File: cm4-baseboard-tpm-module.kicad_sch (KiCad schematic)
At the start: 0 parts

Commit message: [#104798] Add SLB9672 and gpio connector to schematic
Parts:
- added C1, C2, C4: C_100n_25V_0402, antmicro-footprints:C_0402_1005Metric, symbol antmicroCapacitors0402:C_100n_25V_0402
- added C3: C_1u_10V_X7R_0402, antmicro-footprints:C_0402_1005Metric, symbol antmicroCapacitors0402:C_1u_10V_X7R_0402
- added J1: Plug_Samtec_ERM5_2x20_ERM5-020-05.0-L-DV-K-TR, antmicro-footprints:Conn_Plug_Samtec_ERM5_2x20_ERM5-020-05.0-L-DV-K-TR, symbol antmicroB2BConnectors:Plug_Samtec_ERM5_2x20_ERM5-020-05.0-L-DV-K-TR
- added R1, R2, R3, R4, R5, R6, R7, R8, R9: R_0R_0402, antmicro-footprints:R_0402_1005Metric, symbol antmicroResistors0402:R_0R_0402
- added U1: OPTIGA TPM SLB 9672 FW16, antmicro-footprints:QFN-32-1EP_5x5mm, symbol antmicroInterfaceControllers:OPTIGA TPM SLB 9672 FW16
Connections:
- new net: U1.10 (NCI_3), U1.11 (NCI_4), U1.12 (NCI_5), U1.13 (NCI_6), U1.15 (NCI_7), U1.16 (NCI_8/GND), U1.25 (NCI_9), U1.26 (NCI_10), U1.27 (NCI_11), U1.28 (NCI_12), U1.31 (NCI_13), U1.5 (NCI_1), U1.8 (NCI_2/VDD)
- new net: U1.29 (NC2), U1.30 (NC3), U1.6 (NC1)
- new net +3V3: C1.2, C2.2, C3.2, C4.2, J1.1, J1.17, U1.1 (VDD_1), U1.14 (VDD_2), U1.22 (VDD_3)
- new net GND: C1.1, C2.1, C3.1, C4.1, J1.20, J1.25, J1.34, J1.39, J1.6, J1.9, U1.2 (GND_1), U1.23 (GND_3), U1.32 (GND_4), U1.33 (EP), U1.9 (GND_2)
- new net GPIO.0/SDA0: J1.27
- new net GPIO.10: J1.19
- new net GPIO.11: J1.23
- new net GPIO.12/RXD5: J1.32
- new net GPIO.13/TXD5: J1.33
- new net GPIO.14/RXD0: J1.8
- new net GPIO.15/TXD0: J1.10
- new net GPIO.16: J1.36
- new net GPIO.17: J1.11
- new net GPIO.18: J1.12
- new net GPIO.19: J1.35
- new net GPIO.1/SCL0: J1.28
- new net GPIO.2: J1.3
- new net GPIO.20: J1.38
- new net GPIO.21: J1.40
- new net GPIO.22: J1.15
- new net GPIO.23: J1.16
- new net GPIO.24: J1.18
- new net GPIO.25: J1.22
- new net GPIO.26: J1.37
- new net GPIO.27: J1.13
- new net GPIO.3: J1.5
- new net GPIO.4/TXD3: J1.7
- new net GPIO.5/RXD3: J1.29
- new net GPIO.6: J1.31
- new net GPIO.7: J1.26
- new net GPIO.8/TXD4: J1.24
- new net GPIO.9/RXD4: J1.21
- new net GPIO.AIN0: J1.30
- new net GPIO.AIN1: J1.14
- new net GPIO_00: R7.2, U1.3 (GPIO__00)
- new net GPIO_00_R: R7.1
- new net GPIO_01: R8.2, U1.4 (GPIO__01)
- new net GPIO_01_R: R8.1
- new net GPIO_02: R9.2, U1.7 (GPIO__02)
- new net GPIO_02_R: R9.1
- new net SPI.MISO: R3.2, U1.24 (MISO)
- new net SPI.MISO_R: R3.1
- new net SPI.MOSI: R4.2, U1.21 (MOSI)
- new net SPI.MOSI_R: R4.1
- new net SPI.SCLK: R1.2, U1.19 (SCLK)
- new net SPI.SCLK_R: R1.1
- new net SPI.~{CS}: R2.2, U1.20 (CS_N)
- new net SPI.~{CS}_R: R2.1
- new net ~{PIRQ}: R5.2, U1.18 (PIRQ_N)
- new net ~{PIRQ}_R: R5.1
- new net ~{RST}: R6.2, U1.17 (RST_N)
- new net ~{RST}_R: R6.1
- no-connect marks 0 -> 4
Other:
- note added: "5V not supported"
- note added: "CM4 Baseboard connector"
- note added: "Connect to suitable GPIO!"
- note added: "Pin 8 Pulled up to 3V3"
- note added: "Pullup on CS"
- note added: "Symbol and Footprint both need to be changed! Design stays intact"
- note added: "https://www.infineon.com/assets/row/public/documents/30/49/infineon-slb9672-tpm20-spi-fw16.xx-ds-rev1-3-2024-11-18-datasheet-en.pdf https://www.mouser.pl/datasheet/3/70/1/infineon_optiga_tpm_slb_9672_kit_datasheet_en.pdf"

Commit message: [#104798] Update SLB9672 symbol, finish schematic
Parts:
- removed U1: OPTIGA TPM SLB 9672 FW16, antmicro-footprints:QFN-32-1EP_5x5mm, symbol antmicroInterfaceControllers:OPTIGA TPM SLB 9672 FW16
- added C5: C_100n_25V_0402, antmicro-footprints:C_0402_1005Metric, symbol antmicroCapacitors0402:C_100n_25V_0402
- added R10, R11: R_10k_0402, antmicro-footprints:R_0402_1005Metric, symbol antmicroResistors0402:R_10k_0402
- added U2: SLB9672XU20FW1624XTMA1, antmicro-footprints:QFN-32-1EP_5x5mm_P0.5mm, symbol antmicroInterfaceControllers:SLB9672XU20FW1624XTMA1
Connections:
- net GPIO.10 is gone; now on net SPI.SCLK: J1.19
- net GPIO.11 is gone; now on net SPI.SCLK: J1.23
- net GPIO.8/TXD4 is gone; now on net SPI.~{CS}: J1.24
- net GPIO.9/RXD4 is gone; now on net SPI.MISO: J1.21
- net +3V3: now also C5.2, R10.2, R11.2, U2.1 (VDD), U2.14 (VDD), U2.22 (VDD), U2.8 (NCI/VDD)
- net GND: now also C5.1, U2.16 (NCI/GND), U2.33 (EP), U2.[2,9,23,32] (GND)
- net GPIO_00: now also R7.1; no longer R7.2
- net GPIO_00_R: now also R7.2, U2.3 (GPIO__00); no longer R7.1
- net GPIO_01: now also R8.1; no longer R8.2
- net GPIO_01_R: now also R8.2, U2.4 (GPIO__01); no longer R8.1
- net GPIO_02: now also R9.1; no longer R9.2
- net GPIO_02_R: now also R9.2, U2.7 (GPIO__02); no longer R9.1
- net SPI.MISO: now also R3.1; no longer R3.2
- net SPI.MISO_R: now also R3.2, U2.24 (MISO); no longer R3.1
- net SPI.MOSI: now also R4.1; no longer R4.2
- net SPI.MOSI_R: now also R4.2, U2.21 (MOSI); no longer R4.1
- net SPI.SCLK: now also R1.1; no longer R1.2
- net SPI.SCLK_R: now also R1.2, U2.19 (SCLK); no longer R1.1
- net SPI.~{CS}: now also R2.1; no longer R2.2
- net SPI.~{CS}_R: now also R2.2, R10.1, U2.20 (~{CS}); no longer R2.1
- net ~{PIRQ}: now also R5.1; no longer R5.2
- net ~{PIRQ}_R: now also R5.2, U2.18 (~{PIRQ}); no longer R5.1
- net ~{RST}: now also R6.1; no longer R6.2
- net ~{RST}_R: now also R6.2, U2.17 (~{RST}); no longer R6.1
- new net: R11.1, U2.10 (NCI/VDD)
- no-connect marks 4 -> 2
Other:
- note added: "Connect to any GPIO for easier routing"
- note added: "SLB9672 TPM IC"
- note removed: "Connect to suitable GPIO!"
- note removed: "Pin 8 Pulled up to 3V3"
- note removed: "Pullup on CS"
- note removed: "Symbol and Footprint both need to be changed! Design stays intact"
- note removed: "https://www.infineon.com/assets/row/public/documents/30/49/infineon-slb9672-tpm20-spi-fw16.xx-ds-rev1-3-2024-11-18-datasheet-en.pdf https://www.mouser.pl/datasheet/3/70/1/infineon_optiga_tpm_slb_9672_kit_datasheet_en.pdf"
- moved on the sheet: C1, C2, C3, C4, J1, R1, R2, R3, R4, R5, R6, R7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

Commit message: [#104798] Make full placement and layout, clear DRC
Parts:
- added N1001: antmicro_logo, antmicro-footprints:antmicro-logo_scaled_12mm, symbol antmicroMechanicalParts:antmicro_logo
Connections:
- net GPIO.14/RXD0 is gone; now on net ~{RST}: J1.8
- net GPIO.15/TXD0 is gone; now on net ~{PIRQ}: J1.10
- net GPIO.16 is gone; now on net GPIO_00: J1.36
- net GPIO.20 is gone; now on net GPIO_01: J1.38
- net GPIO.21 is gone; now on net GPIO_02: J1.40
- net SPI.MOSI: now also J1.19
- net SPI.SCLK: no longer J1.19
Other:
- note removed: "Connect to any GPIO for easier routing"
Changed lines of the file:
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@@
 		)
 	)
-	(text "Connect to any GPIO for easier routing"
-		(exclude_from_sim no)
-		(at 187.452 161.036 0)
-		(effects
-			(font
-				(size 1.27 1.27)
-			)
-		)
-	)
 	(junction
 		(at 303.53 124.46)
@@
 	(wire
 		(pts
-			(xy 142.24 161.29) (xy 160.02 161.29)
-		)
-		(stroke
-			(width 0)
-			(type default)
-		)
-	)
-	(wire
-		(pts
 			(xy 209.55 163.83) (xy 222.25 163.83)
 		)
@@
 		)
 	)
-	(wire
-		(pts
-			(xy 142.24 158.75) (xy 160.02 158.75)
-		)
-		(stroke
-			(width 0)
-			(type default)
-		)
-	)
 	(bus
 		(pts
@@
 	(wire
 		(pts
+			(xy 142.24 161.29) (xy 160.02 161.29)
+		)
+		(stroke
+			(width 0)
+			(type default)
+		)
+	)
+	(wire
+		(pts
 			(xy 142.24 135.89) (xy 160.02 135.89)
 		)
@@
 	(wire
 		(pts
-			(xy 113.03 161.29) (xy 130.81 161.29)
+			(xy 142.24 158.75) (xy 160.02 158.75)
 		)
 		(stroke
@@
 	(wire
 		(pts
-			(xy 209.55 157.48) (xy 222.25 157.48)
+			(xy 113.03 161.29) (xy 130.81 161.29)
 		)
 		(stroke
@@
 	(wire
 		(pts
-			(xy 332.74 133.35) (xy 332.74 135.89)
+			(xy 209.55 157.48) (xy 222.25 157.48)
 		)
 		(stroke
@@
 	(wire
 		(pts
-			(xy 113.03 158.75) (xy 130.81 158.75)
+			(xy 332.74 133.35) (xy 332.74 135.89)
 		)
 		(stroke
@@
 	(wire
 		(pts
-			(xy 303.53 133.35) (xy 303.53 132.08)
+			(xy 113.03 158.75) (xy 130.81 158.75)
 		)
 		(stroke
@@
 	(wire
 		(pts
-			(xy 227.33 154.94) (xy 247.65 154.94)
+			(xy 303.53 133.35) (xy 303.53 132.08)
 		)
 		(stroke
@@
 	(wire
 		(pts
-			(xy 227.33 157.48) (xy 247.65 157.48)
+			(xy 227.33 154.94) (xy 247.65 154.94)
 		)
 		(stroke
@@
 	(wire
 		(pts
-			(xy 113.03 168.91) (xy 130.81 168.91)
+			(xy 227.33 157.48) (xy 247.65 157.48)
 		)
 		(stroke
@@
 	(wire
 		(pts
-			(xy 142.24 156.21) (xy 160.02 156.21)
+			(xy 113.03 168.91) (xy 130.81 168.91)
 		)
 		(stroke
@@
 	(wire
 		(pts
-			(xy 113.03 163.83) (xy 130.81 163.83)
+			(xy 142.24 153.67) (xy 160.02 153.67)
 		)
 		(stroke
@@
 	(wire
 		(pts
-			(xy 142.24 153.67) (xy 160.02 153.67)
+			(xy 113.03 163.83) (xy 130.81 163.83)
 		)
 		(stroke
@@
 	(wire
 		(pts
+			(xy 142.24 156.21) (xy 160.02 156.21)
+		)
+		(stroke
+			(width 0)
+			(type default)
+		)
+	)
+	(wire
+		(pts
 			(xy 227.33 146.05) (xy 247.65 146.05)
 		)
@@
 		)
 	)
+	(label "GPIO_00"
+		(at 160.02 166.37 180)
+		(effects
+			(font
+				(size 1.27 1.27)
+			)
+			(justify right bottom)
+		)
+	)
 	(label "SPI.SCLK_R"
 		(at 234.95 140.97 0)
@@
 		)
 	)
-	(label "GPIO.14/RXD0"
-		(at 160.02 130.81 180)
-		(effects
-			(font
-				(size 1.27 1.27)
-			)
-			(justify right bottom)
-		)
-	)
 	(label "GPIO.24"
 		(at 160.02 143.51 180)
@@
 		)
 	)
-	(label "GPIO.20"
-		(at 160.02 168.91 180)
-		(effects
-			(font
-				(size 1.27 1.27)
-			)
-			(justify right bottom)
-		)
-	)
 	(label "GPIO.25"
 		(at 160.02 148.59 180)
@@
 		)
 	)
-	(label "SPI.SCLK"
-		(at 113.03 146.05 0)
-		(effects
-			(font
-				(size 1.27 1.27)
-			)
-			(justify left bottom)
-		)
-	)
 	(label "~{RST}_R"
 		(at 234.95 157.48 0)
@@
 		)
 	)
-	(label "GPIO.15/TXD0"
-		(at 160.02 133.35 180)
-		(effects
-			(font
-				(size 1.27 1.27)
-			)
-			(justify right bottom)
-		)
-	)
 	(label "GPIO_02"
 		(at 209.55 168.91 0)
@@
 		)
 	)
+	(label "GPIO_02"
+		(at 160.02 171.45 180)
+		(effects
+			(font
+				(size 1.27 1.27)
+			)
+			(justify right bottom)
+		)
+	)
 	(label "GPIO_00_R"
 		(at 234.95 163.83 0)
@@
 		)
 	)
-	(label "GPIO.21"
-		(at 160.02 171.45 180)
+	(label "GPIO_01"
+		(at 160.02 168.91 180)
 		(effects
 			(font
@@
 		)
 	)
-	(label "GPIO.16"
-		(at 160.02 166.37 180)
-		(effects
-			(font
-				(size 1.27 1.27)
-			)
-			(justify right bottom)
-		)
-	)
 	(label "GPIO.1{slash}SCL0"
 		(at 160.02 156.21 180)
@@
 		)
 	)
+	(label "~{RST}"
+		(at 160.02 130.81 180)
+		(effects
+			(font
+				(size 1.27 1.27)
+			)
+			(justify right bottom)
+		)
+	)
 	(label "GPIO.7"
 		(at 160.02 153.67 180)
@@
 		)
 	)
+	(label "~{PIRQ}"
+		(at 160.02 133.35 180)
+		(effects
+			(font
+				(size 1.27 1.27)
+			)
+			(justify right bottom)
+		)
+	)
 	(label "~{PIRQ}_R"
 		(at 234.95 154.94 0)
@@
 		)
 	)
+	(label "SPI.MOSI"
+		(at 113.03 146.05 0)
+		(effects
+			(font
+				(size 1.27 1.27)
+			)
+			(justify left bottom)
+		)
+	)
 	(label "GPIO.18"
 		(at 160.02 135.89 180)
@@
 					(unit 1)
 				)
+			)
+		)
+	)
+	(symbol
+		(lib_id "antmicroMechanicalParts:antmicro_logo")
+		(at 308.61 173.99 0)
+		(unit 1)
+		(body_style 1)
+		(exclude_from_sim no)
+		(in_bom no)
+		(on_board yes)
+		(in_pos_files yes)
+		(dnp no)
+		(fields_autoplaced yes)
+		(property "Reference" "N1001"
+			(at 314.96 172.0062 0)
+			(show_name no)
+			(do_not_autoplace no)
+			(effects
+				(font
+					(size 1.27 1.27)
+					(thickness 0.15)
+				)
+				(justify left)
+			)
+		)
+		(property "Value" "antmicro_logo"
+			(at 314.96 174.5462 0)
+			(show_name no)
+			(do_not_autoplace no)
+			(effects
+				(font
+					(size 1.27 1.27)
+					(thickness 0.15)
+				)
+				(justify left)
+			)
+		)
+		(property "Footprint" "antmicro-footprints:antmicro-logo_scaled_12mm"
+			(at 323.85 184.15 0)
+			(hide yes)
+			(show_name no)
+			(do_not_autoplace no)
+			(effects
+				(font
+					(size 1.27 1.27)
+					(thickness 0.15)
+				)
+				(justify left bottom)
+			)
+		)
+		(property "Datasheet" ""
+			(at 323.85 186.69 0)
+			(hide yes)
+			(show_name no)
+			(do_not_autoplace no)
+			(effects
+				(font
+					(size 1.27 1.27)
+					(thickness 0.15)
+				)
+				(justify left bottom)
+			)
+		)
+		(property "Description" "Mechanical part"
+			(at 323.85 196.85 0)
+			(hide yes)
+			(show_name no)
+			(do_not_autoplace no)
+			(effects
+				(font
+					(size 1.27 1.27)
+				)
+				(justify left bottom)
+			)
+		)
+		(property "MPN" ""
+			(at 308.61 173.99 0)
+			(show_name no)
+			(do_not_autoplace no)
+			(effects
+				(font
+					(size 1.27 1.27)
+				)
+			)
+		)
+		(property "Manufacturer" ""
+			(at 323.85 194.31 0)
+			(hide yes)
+			(show_name no)
+			(do_not_autoplace no)
+			(effects
+				(font
+					(size 1.27 1.27)
+					(thickness 0.15)
+				)
+				(justify left bottom)
+			)
+		)
+		(property "Author" "Antmicro"
+			(at 323.85 189.23 0)
+			(hide yes)
+			(show_name no)
+			(do_not_autoplace no)
+			(effects
+				(font
+					(size 1.27 1.27)
+					(thickness 0.15)
+				)
+				(justify left bottom)
+			)
+		)
+		(property "License" "Apache-2.0"
+			(at 323.85 191.77 0)
+			(hide yes)
+			(show_name no)
+			(do_not_autoplace no)
+			(effects
+				(font
+					(size 1.27 1.27)
+					(thickness 0.15)
+				)
+				(justify left bottom)
+			)
+		)
+		(instances
+			(project "cm4-baseboard-tpm-module"
+				(path "/14d39343-e453-4480-a79e-bc08955afca3"
+					(reference "N1001")
+					(unit 1)
+				)

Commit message: [#104798] Add measurements, bump date
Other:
- moved on the sheet: N1001
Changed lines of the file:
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@@
 	(symbol
 		(lib_id "antmicroMechanicalParts:antmicro_logo")
-		(at 308.61 173.99 0)
+		(at 300.99 171.45 0)
 		(unit 1)
 		(body_style 1)
@@
 		(fields_autoplaced yes)
 		(property "Reference" "N1001"
-			(at 314.96 172.0062 0)
+			(at 307.34 169.4662 0)
 			(show_name no)
 			(do_not_autoplace no)
@@
 		)
 		(property "Value" "antmicro_logo"
-			(at 314.96 174.5462 0)
+			(at 307.34 172.0062 0)
 			(show_name no)
 			(do_not_autoplace no)
@@
 		)
 		(property "Footprint" "antmicro-footprints:antmicro-logo_scaled_12mm"
-			(at 323.85 184.15 0)
+			(at 316.23 181.61 0)
 			(hide yes)
 			(show_name no)
@@
 		)
 		(property "Datasheet" ""
-			(at 323.85 186.69 0)
+			(at 316.23 184.15 0)
 			(hide yes)
 			(show_name no)
@@
 		)
 		(property "Description" "Mechanical part"
-			(at 323.85 196.85 0)
+			(at 316.23 194.31 0)
 			(hide yes)
 			(show_name no)
@@
 		)
 		(property "MPN" ""
-			(at 308.61 173.99 0)
+			(at 300.99 171.45 0)
 			(show_name no)
 			(do_not_autoplace no)
@@
 		)
 		(property "Manufacturer" ""
-			(at 323.85 194.31 0)
+			(at 316.23 191.77 0)
 			(hide yes)
 			(show_name no)
@@
 		)
 		(property "Author" "Antmicro"
-			(at 323.85 189.23 0)
+			(at 316.23 186.69 0)
 			(hide yes)
 			(show_name no)
@@
 		)
 		(property "License" "Apache-2.0"
-			(at 323.85 191.77 0)
+			(at 316.23 189.23 0)
 			(hide yes)
 			(show_name no)

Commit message: [#104798] Change board dimensions, add VCC LED, OSHW logo, ficudials and testpoints
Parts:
- added D1: LED_G_0603_KP-1608CGCK, antmicro-footprints:LED_0603_1608Metric_G, symbol antmicroLEDIndicationDiscrete:LED_G_0603_KP-1608CGCK
- added FD1, FD2: Fiducial_1mm_Mask2mm, antmicro-footprints:Fiducial_1mm_Mask2mm, symbol antmicroFiducialMarks:Fiducial_1mm_Mask2mm
- added MP1, MP2: MP_NPTH_Drill3.2mm, antmicro-footprints:MP_NPTH_Drill3.2mm, symbol antmicroMechanicalParts:MP_NPTH_Drill3.2mm
- added N2: oshw_logo, antmicro-footprints:oshw-logo, symbol antmicroMechanicalParts:oshw_logo
- added R12: R_470R_0402, antmicro-footprints:R_0402_1005Metric, symbol antmicroResistors0402:R_470R_0402
- added TP1, TP2: TP_Pad0.75mm_Drill0.2mm, antmicro-footprints:TP_Pad0.75mm_Drill0.2mm, symbol antmicroTestPoints:TP_Pad0.75mm_Drill0.2mm
- renumbered C5 to C1, C1 to C2, C2 to C3, C3 to C5, N1001 to N1, U2 to U1
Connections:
- net +3V3: now also R12.2, TP2.1
- net GND: now also D1.1 (C), TP1.1
- new net: D1.2 (A), R12.1
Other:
- note added: "GPIO max current = 1mA Driving LED needs a transistor"

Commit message: [#104798] Clear DRC
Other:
- note removed: "GPIO max current = 1mA Driving LED needs a transistor"
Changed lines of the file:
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@@
-		)
-	)
-	(text "GPIO max current = 1mA\nDriving LED needs a transistor"
-		(exclude_from_sim no)
-		(at 227.838 175.514 0)
-		(effects
-			(font
-				(size 1.27 1.27)
-			)
 		)
 	)

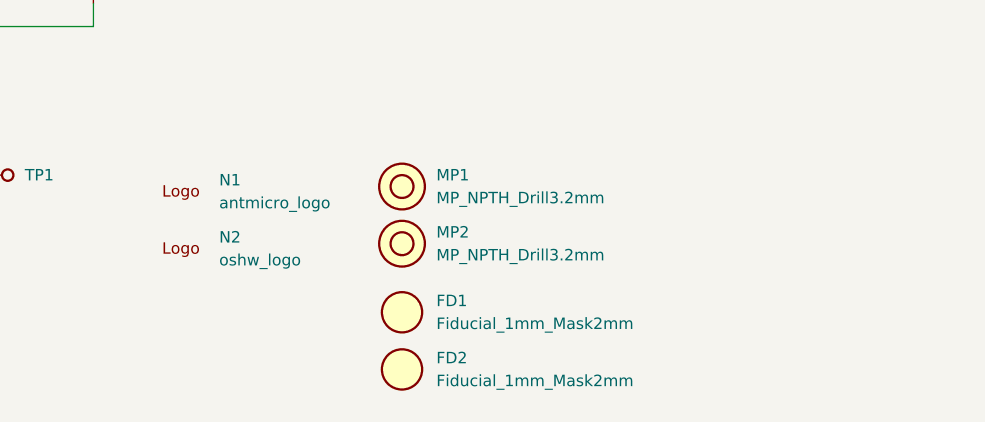
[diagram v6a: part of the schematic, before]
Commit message: [#104798] Add testpoints and reroute the PCB
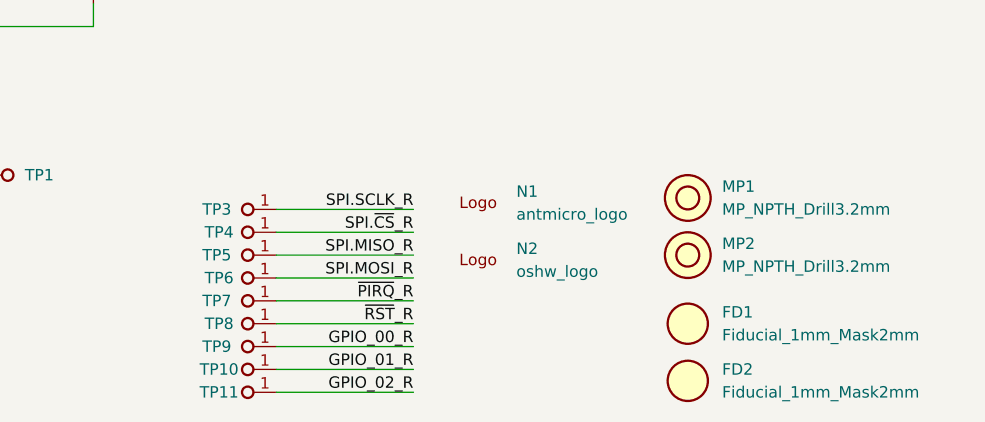
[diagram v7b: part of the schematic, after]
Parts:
- added TP10, TP11, TP3, TP4, TP5, TP6, TP7, TP8, TP9: TP_Pad0.75mm_Drill0.2mm, antmicro-footprints:TP_Pad0.75mm_Drill0.2mm, symbol antmicroTestPoints:TP_Pad0.75mm_Drill0.2mm
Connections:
- net GPIO_00_R: now also TP9.1
- net GPIO_01_R: now also TP10.1
- net GPIO_02_R: now also TP11.1
- net SPI.MISO_R: now also TP5.1
- net SPI.MOSI_R: now also TP6.1
- net SPI.SCLK_R: now also TP3.1
- net SPI.~{CS}_R: now also TP4.1
- net ~{PIRQ}_R: now also TP7.1
- net ~{RST}_R: now also TP8.1
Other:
- moved on the sheet: FD1, FD2, MP1, MP2, N1, N2
